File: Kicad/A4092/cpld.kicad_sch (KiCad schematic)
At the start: 27 parts, among them J8 Conn_01x06_Pin, U13 W25X40CLSN, U7 AMS1117-3.3, U8 XC95144XL-TQ144, Y1 Abracon ACO-50MHz, Y2 Abracon ACO-40MHz

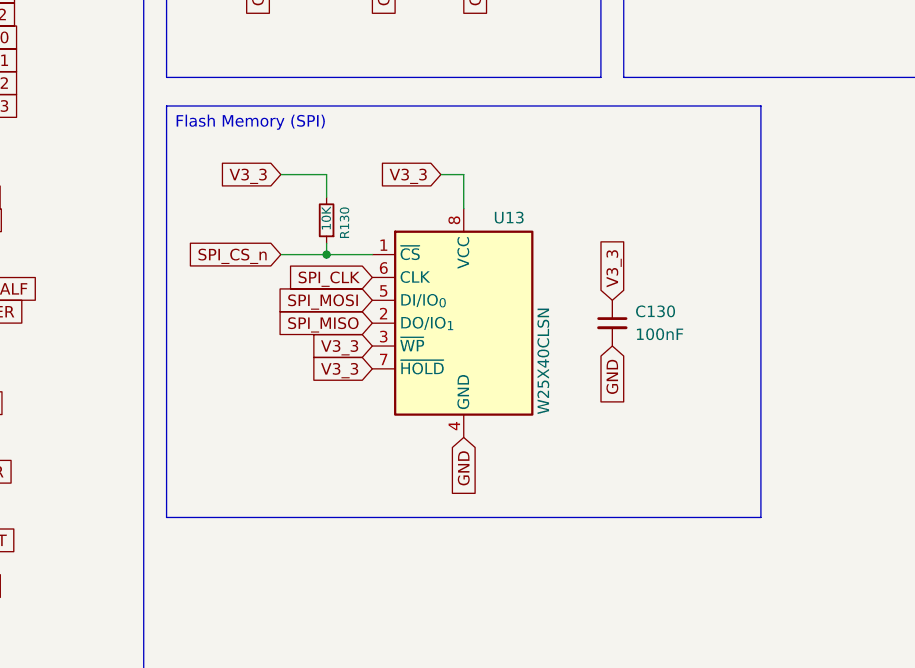
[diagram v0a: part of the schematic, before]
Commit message: Add series resistors for SPI
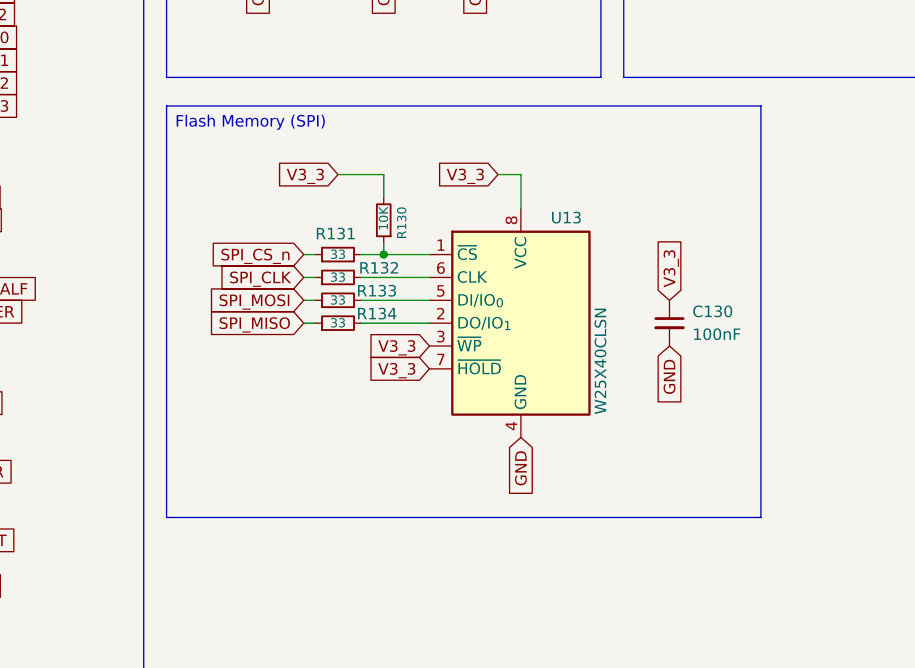
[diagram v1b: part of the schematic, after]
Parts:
- added R131, R132, R133, R134: 33, Resistor_SMD:R_0603_1608Metric, symbol Device:R_Small
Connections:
- net SPI_CLK: now also R132.1; no longer U13.6 (CLK)
- net SPI_CS_n: now also R131.1; no longer R130.1, U13.1 (~{CS})
- net SPI_MISO: now also R134.1; no longer U13.2 (DO/IO_{1})
- net SPI_MOSI: now also R133.1; no longer U13.5 (DI/IO_{0})
- new net: R132.2, U13.6 (CLK)
- new net: R133.2, U13.5 (DI/IO_{0})
- new net: R130.1, R131.2, U13.1 (~{CS})
- new net: R134.2, U13.2 (DO/IO_{1})
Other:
- moved on the sheet: C130, R130, U13

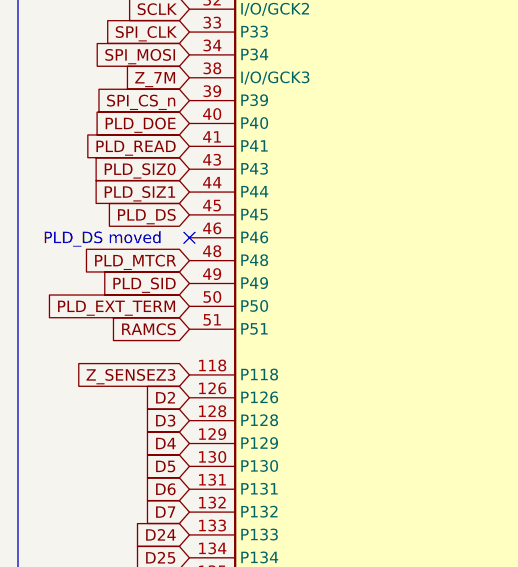
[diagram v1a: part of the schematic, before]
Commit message: Mark PLD_SID as NC on U8
Pin 91 on U8 (PLD_SID) is now unused because there is no
more DIP switch logic on the board.
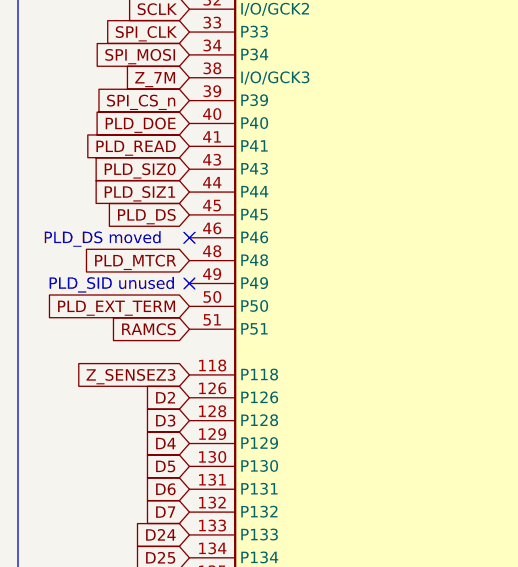
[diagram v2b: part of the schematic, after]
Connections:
- net PLD_SID: no longer names the net of U8.49 (P49)
- no-connect marks 10 -> 11
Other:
- note added: "PLD_SID unused"
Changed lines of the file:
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@@
+		)
+	)
+	(text "PLD_SID unused"
+		(exclude_from_sim no)
+		(at 25.654 134.874 0)
+		(effects
+			(font
+				(size 1.27 1.27)
+			)
 		)
 	)
@@
 	)
 	(no_connect
+		(at 34.29 134.62)
+	)
+	(no_connect
 		(at 195.58 63.5)
 	)
@@
 				(hide yes)
 			)
-		)
-	)
-	(global_label "PLD_SID"
-		(shape input)
-		(at 34.29 134.62 180)
-		(fields_autoplaced yes)
-		(effects
-			(font
-				(size 1.27 1.27)
-			)
-			(justify right)
-		)
-		(property "Intersheetrefs" "${INTERSHEET_REFS}"
-			(at 23.6848 134.62 0)
-			(effects
-				(font
-					(size 1.27 1.27)
-				)
-				(justify right)
-				(hide yes)
-			)

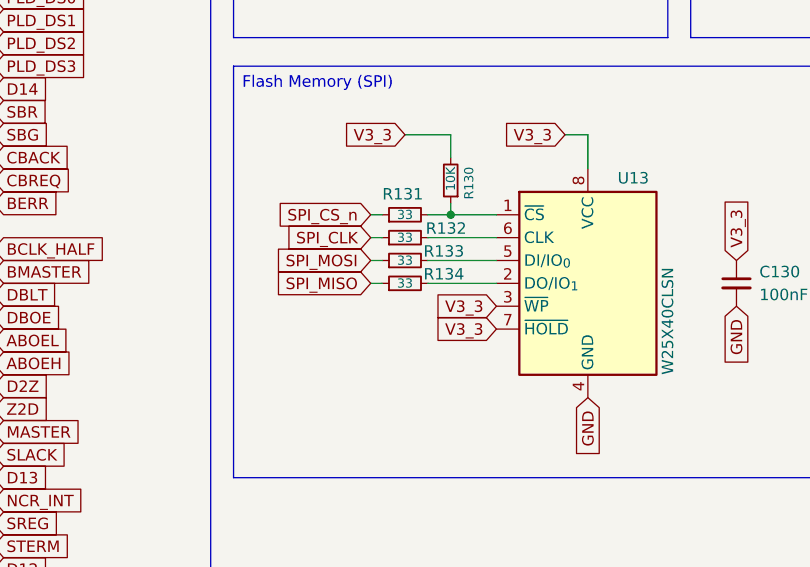
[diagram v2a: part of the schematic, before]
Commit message: Series resistor for MISO 33O -> 0O
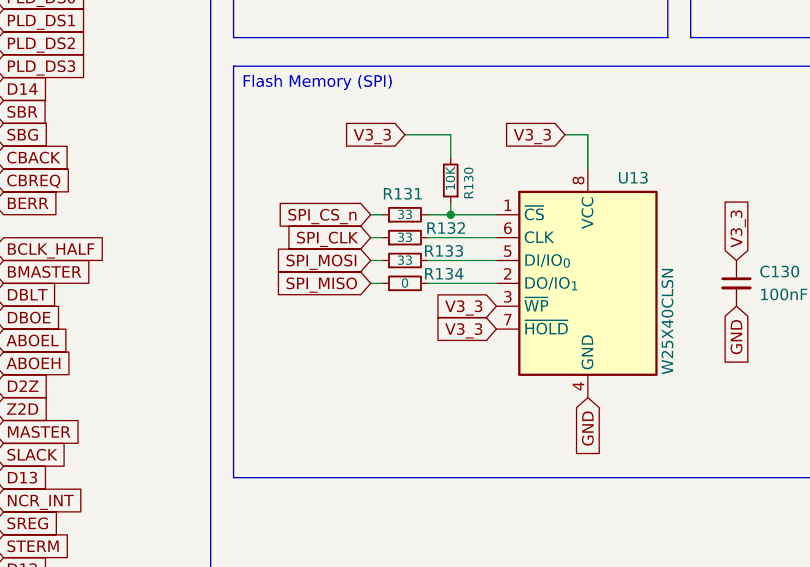
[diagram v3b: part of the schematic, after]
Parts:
- R134: value 33 -> 0
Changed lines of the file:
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@@
 			)
 		)
-		(property "Value" "33"
+		(property "Value" "0"
 			(at 146.05 140.97 90)
 			(effects

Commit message: Clean up pull-up resistors
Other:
- title: A4092 -> Cheetah UW
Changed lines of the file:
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@@
 	(paper "A4")
 	(title_block
-		(title "A4092")
-		(rev "PROTO0")
+		(title "Cheetah UW")
+		(rev "PROTO1")
 		(company "amiga.technology")
 	)

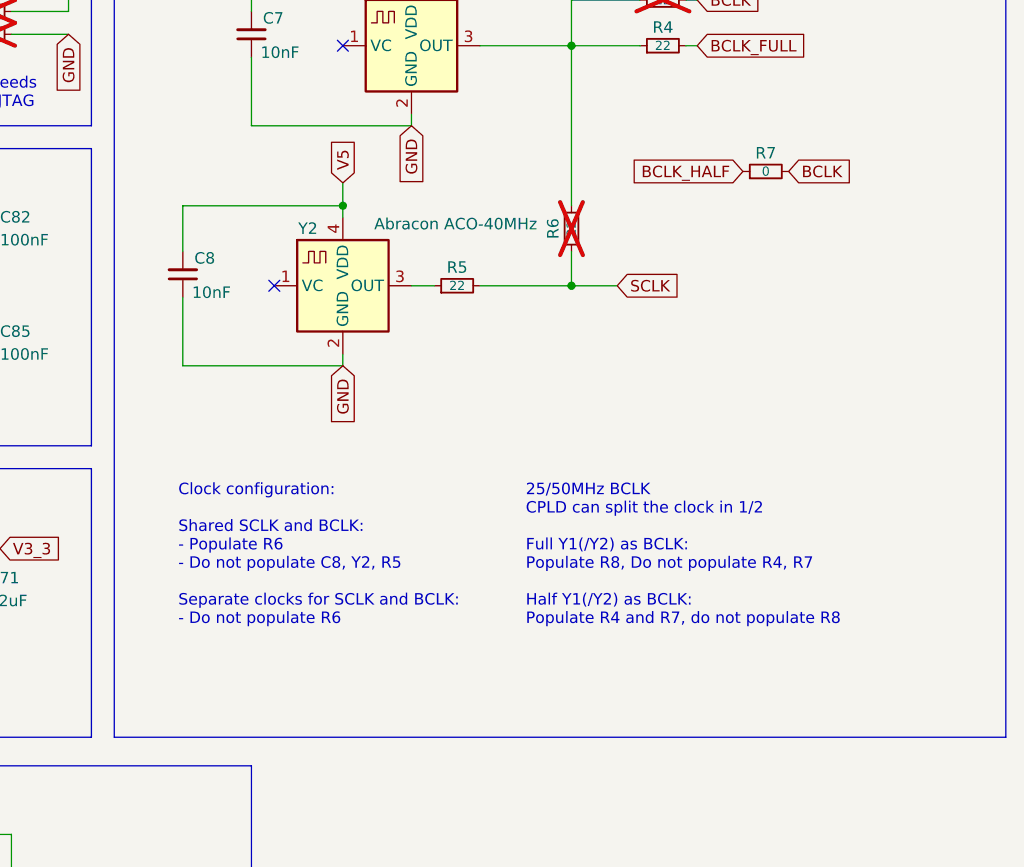
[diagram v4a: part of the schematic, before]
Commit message: Add more clarity around clock circuit
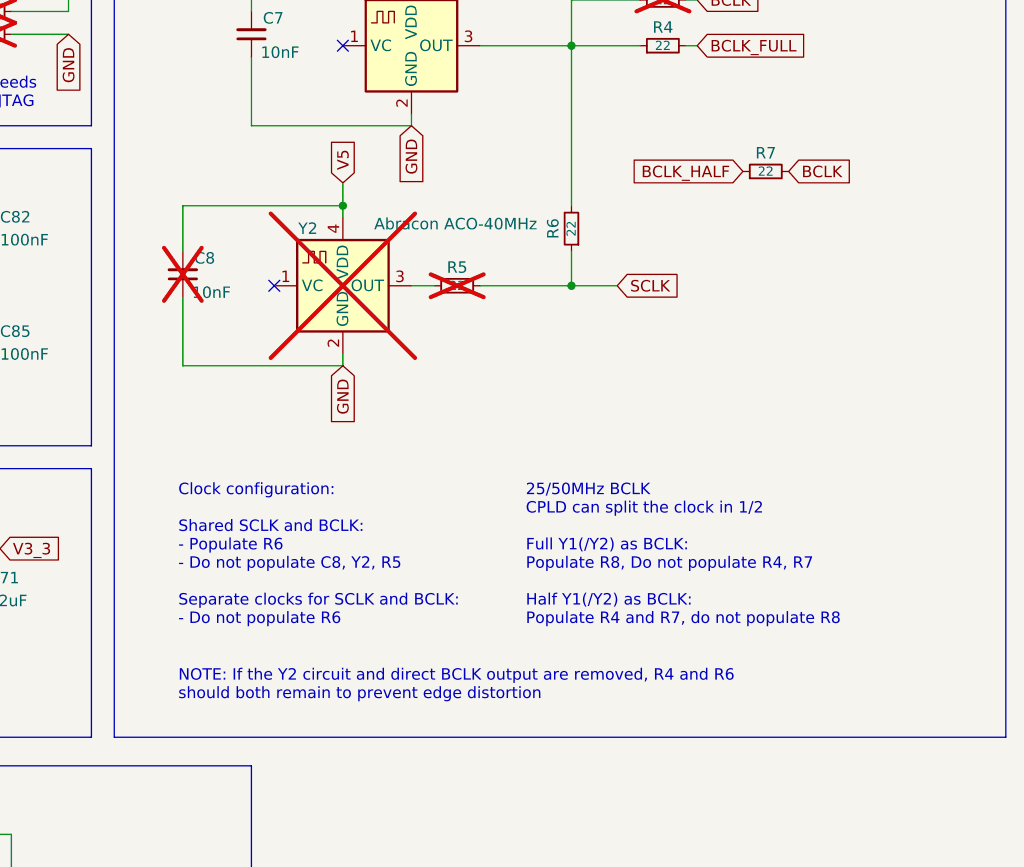
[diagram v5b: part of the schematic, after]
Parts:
- C8, R5, Y2: now not fitted; now left out of the parts list
- R6: now fitted
- R7: value 0 -> 22
- R8: now left out of the parts list
- R83: footprint Resistor_SMD:R_0603_1608Metric_Pad0.98x0.95mm_HandSolder -> R131
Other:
- note added: "NOTE: If the Y2 circuit and direct BCLK output are removed, R4 and R6 should both remain to prevent edge distortion"
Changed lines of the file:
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@@
 		(company "amiga.technology")
 	)
+	(text "NOTE: If the Y2 circuit and direct BCLK output are removed, R4 and R6 \nshould both remain to prevent edge distortion"
+		(exclude_from_sim no)
+		(at 184.912 107.95 0)
+		(effects
+			(font
+				(size 1.27 1.27)
+			)
+			(justify left)
+		)
+	)
 	(text "Clock configuration:\n\nShared SCLK and BCLK:\n- Populate R6\n- Do not populate C8, Y2, R5\n\nSeparate clocks for SCLK and BCLK:\n- Do not populate R6\n"
 		(exclude_from_sim no)
@@
 		(unit 1)
 		(exclude_from_sim no)
-		(in_bom yes)
+		(in_bom no)
 		(on_board yes)
-		(dnp no)
+		(dnp yes)
 		(property "Reference" "C8"
 			(at 186.69 60.452 0)
@@
 		(unit 1)
 		(exclude_from_sim no)
-		(in_bom yes)
+		(in_bom no)
 		(on_board yes)
 		(dnp yes)
@@
 			)
 		)
-		(property "Value" "0"
+		(property "Value" "22"
 			(at 250.19 50.8 90)
 			(effects
@@
 		(in_bom yes)
 		(on_board yes)
-		(dnp yes)
+		(dnp no)
 		(property "Reference" "R6"
 			(at 226.568 57.15 90)
@@
 			)
 		)
-		(property "Footprint" "Resistor_SMD:R_0603_1608Metric_Pad0.98x0.95mm_HandSolder"
+		(property "Footprint" "R131"
 			(at 163.83 33.02 0)
 			(effects
@@
 		(unit 1)
 		(exclude_from_sim no)
-		(in_bom yes)
+		(in_bom no)
 		(on_board yes)
-		(dnp no)
+		(dnp yes)
 		(property "Reference" "R5"
 			(at 215.9 61.468 90)
@@
 		(unit 1)
 		(exclude_from_sim no)
-		(in_bom yes)
+		(in_bom no)
 		(on_board yes)
-		(dnp no)
+		(dnp yes)
 		(property "Reference" "Y2"
 			(at 200.406 57.15 0)

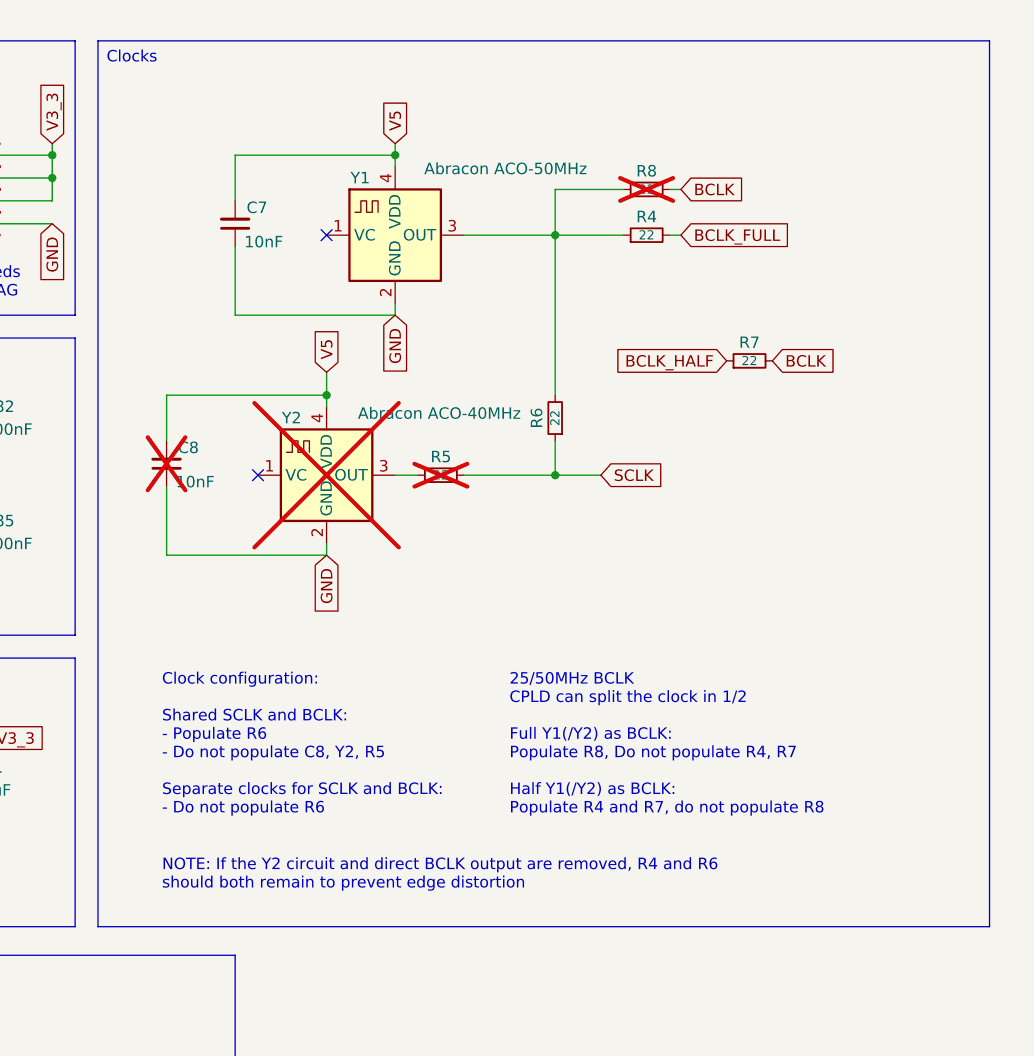
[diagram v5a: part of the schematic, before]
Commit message: Rehaul clock circuit in schematics
and try to add most of the LCSC part numbers
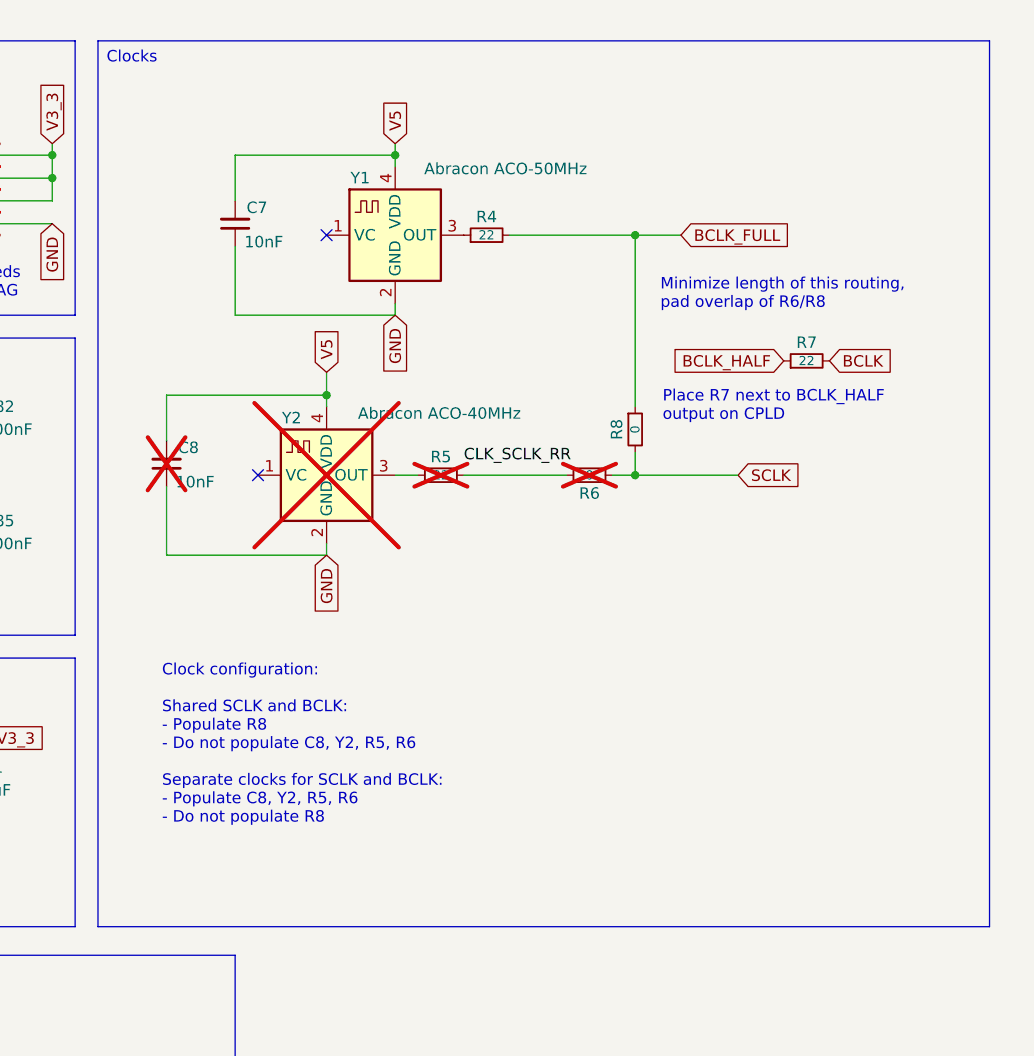
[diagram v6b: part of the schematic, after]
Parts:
- R131, R132, R133: LCSC Part # C108661 -> C23140
- R134: LCSC Part # C108661 -> C21189
- R6: value 22 -> 0; LCSC Part # C23345 -> C21189; now not fitted; now left out of the parts list
- R8: value 22 -> 0; LCSC Part # C23345 -> C21189; now fitted; now in the parts list
- R81, R82, R83, R84: LCSC Part # (none) -> C25804
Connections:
- net BCLK: no longer R8.2
- net BCLK_FULL: now also R8.1
- net SCLK: now also R8.2; no longer R5.2
- net at R4.1, Y1.3 (OUT): no longer R6.2, R8.1
- new net: R5.2, R6.2
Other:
- note added: "Clock configuration: Shared SCLK and BCLK: - Populate R8 - Do not populate C8, Y2, R5, R6 Separate clocks for SCLK and BCLK: - Populate C8, Y2, R5, R6 - Do not populate R8"
- note added: "Minimize length of this routing, pad overlap of R6/R8"
- note added: "Place R7 next to BCLK_HALF output on CPLD"
- note removed: "25/50MHz BCLK CPLD can split the clock in 1/2 Full Y1(/Y2) as BCLK: Populate R8, Do not populate R4, R7 Half Y1(/Y2) as BCLK: Populate R4 and R7, do not populate R8"
- note removed: "Clock configuration: Shared SCLK and BCLK: - Populate R6 - Do not populate C8, Y2, R5 Separate clocks for SCLK and BCLK: - Do not populate R6"
- note removed: "NOTE: If the Y2 circuit and direct BCLK output are removed, R4 and R6 should both remain to prevent edge distortion"
- moved on the sheet: R4, R7
